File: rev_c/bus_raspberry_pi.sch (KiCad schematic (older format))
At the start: 46 parts, among them J1 TERMINATE_JUMPER, J2 LED_JUMPER, SW1 MJTP1243, U1 MCP7940, U2 74HC08, U3 MCP2562, U4 L78L05AC, U5 ATMEGA324_DIP40, U6 L78L33AC, U7 MCP24XX32A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

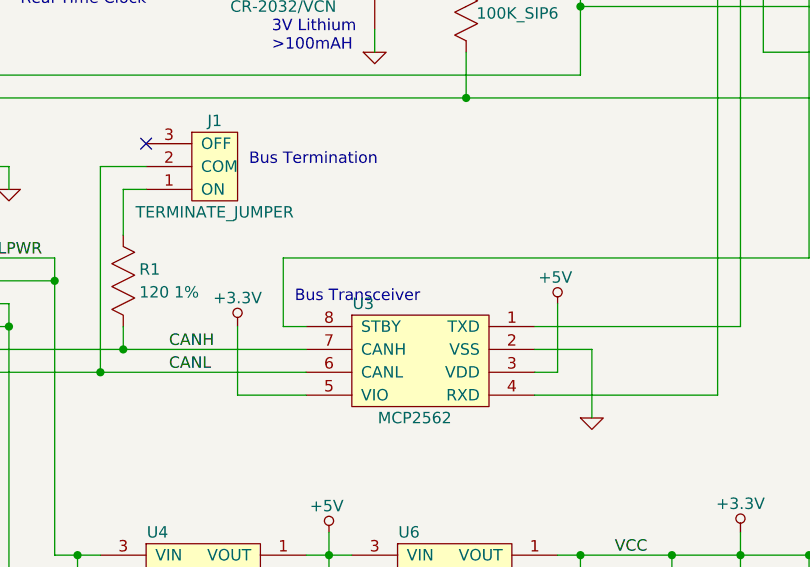
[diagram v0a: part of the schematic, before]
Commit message: Changed from B=>C.  Flipped N1.
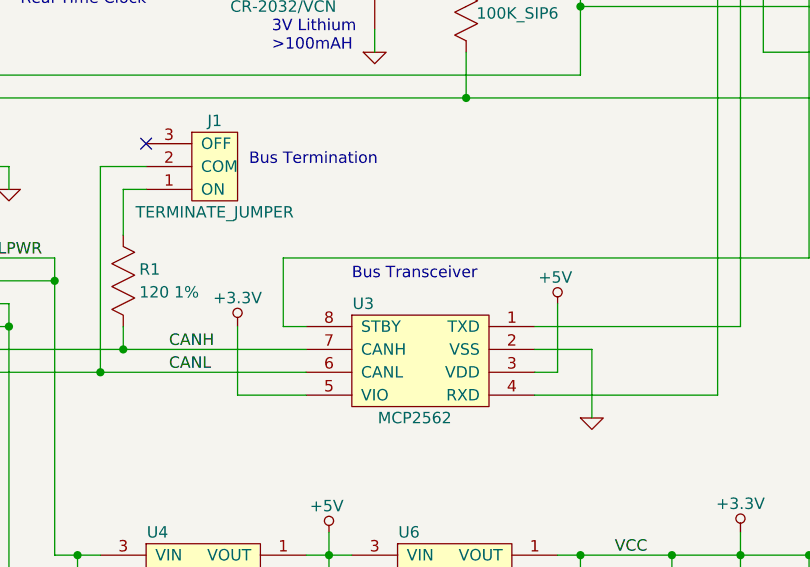
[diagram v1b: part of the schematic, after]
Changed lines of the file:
@@
 Sheet 1 1
 Title "Bus Raspberry Pi"
-Date "Tue 13 Jan 2015"
-Rev "B"
+Date "Sat 31 Jan 2015"
+Rev "C"
 Comp ""
 Comment1 ""
@@
 Text Notes 4500 7800 0    50   ~ 0
 Filter Capacitors
-Text Notes 2650 6000 0    50   ~ 0
+Text Notes 2900 5900 0    50   ~ 0
 Bus Transceiver
 Text Notes 2600 1900 0    50   ~ 0

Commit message: Minor changes to Rev. C.
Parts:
- removed C10: .1uF, bus_raspberry_pi:Capacitor3MMDiscRM2.5, symbol C_HORIZ
- added J3: RESET_SEL, bus_raspberry_pi:Pin_Header_Straight_1x03, symbol RESET_SEL
- added R7: 100K, bus_raspberry_pi:Resistor_Horizontal__400, symbol R_VERT
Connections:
- net +3.3V: now also R7.2; no longer U2.1
- net ~RESET: now also J3.3 (RES); no longer N7.5 (~RESET)
- net at U5.3 (PB2/INT2): now also J3.1 (PGM)
- new net: J3.2 (COM), N7.5 (~RESET)
- new net: R7.1, U2.1
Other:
- moved on the sheet: C6, D1, H5, R2A, R3, U2A
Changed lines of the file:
@@
 Sheet 1 1
 Title "Bus Raspberry Pi"
-Date "Sat 31 Jan 2015"
+Date "Sun 08 Feb 2015"
 Rev "C"
 Comp ""
@@
 L OSHW_LOGO H5
 U 1 1 53E3C102
-P 1000 1100
-F 0 "H5" H 1000 1350 50  0000 C CNN
-F 1 "OSHW_LOGO" H 1000 850 50  0000 C CNN
-F 2 "bus_raspberry_pi:OSHW_LOGO_250mil" H 1000 1100 50  0001 C CNN
-F 3 "" H 1000 1100 50  0000 C CNN
-	1    1000 1100
+P 900 4250
+F 0 "H5" H 900 4500 50  0000 C CNN
+F 1 "OSHW_LOGO" H 900 4000 50  0000 C CNN
+F 2 "bus_raspberry_pi:OSHW_LOGO_250mil" H 900 4250 50  0001 C CNN
+F 3 "" H 900 4250 50  0000 C CNN
+	1    900  4250
 	1    0    0    -1
 $EndComp
@@
 L C_HORIZ C6
 U 1 1 53E3D418
-P 3300 1500
-F 0 "C6" H 3360 1560 50  0000 L CNN
-F 1 ".1uF" H 3360 1430 50  0000 L CNN
-F 2 "bus_raspberry_pi:Capacitor3MMDiscRM2.5" H 3338 1350 30  0001 C CNN
-F 3 "" H 3300 1500 60  0000 C CNN
-	1    3300 1500
+P 3100 1500
+F 0 "C6" H 3160 1560 50  0000 L CNN
+F 1 ".1uF" H 3160 1430 50  0000 L CNN
+F 2 "bus_raspberry_pi:Capacitor3MMDiscRM2.5" H 3138 1350 30  0001 C CNN
+F 3 "" H 3100 1500 60  0000 C CNN
+	1    3100 1500
 	1    0    0    -1
 $EndComp
@@
 L R_VERT R3
 U 1 1 53E3D54A
-P 3600 1200
-F 0 "R3" H 3670 1250 50  0000 L CNN
-F 1 "10K" H 3670 1150 50  0000 L CNN
-F 2 "bus_raspberry_pi:Resistor_Horizontal__400" H 3600 1250 60  0001 C CNN
-F 3 "" H 3600 1250 60  0000 C CNN
-	1    3600 1200
+P 3400 1100
+F 0 "R3" H 3470 1150 50  0000 L CNN
+F 1 "10K" H 3470 1050 50  0000 L CNN
+F 2 "bus_raspberry_pi:Resistor_Horizontal__400" H 3400 1150 60  0001 C CNN
+F 3 "" H 3400 1150 60  0000 C CNN
+	1    3400 1100
 	1    0    0    -1
 $EndComp
@@
 L SCHOTTKY_DIODE_VERT D1
 U 1 1 53E3D5A6
-P 3950 1150
-F 0 "D1" H 3900 1000 50  0000 C CNN
-F 1 "SD101C-TR" H 3700 1250 50  0000 C CNN
-F 2 "bus_raspberry_pi:Diode_DO-41_SOD81_Horizontal_RM10" H 3950 1150 60  0001 C CNN
-F 3 "" H 3950 1150 60  0000 C CNN
-	1    3950 1150
+P 3700 1150
+F 0 "D1" H 3650 1000 50  0000 C CNN
+F 1 "SD101C-TR" H 3450 1250 50  0000 C CNN
+F 2 "bus_raspberry_pi:Diode_DO-41_SOD81_Horizontal_RM10" H 3700 1150 60  0001 C CNN
+F 3 "" H 3700 1150 60  0000 C CNN
+	1    3700 1150
 	-1   0    0    1
 $EndComp
@@
 F 0 "N5" H 850 5950 50  0000 C CNN
 F 1 "FTDI_HEADER" H 950 5125 50  0000 C CNN
-F 2 "bus_raspberry_pi:Pin_Header_Straight_1x06" H 950 5350 60  0001 C CNN
+F 2 "bus_raspberry_pi:Pin_Header_Straight_1x06" H 950 5350 60  0000 C CNN
 F 3 "" H 950 5350 60  0000 C CNN
 	1    950  5350
@@
 NoConn ~ 5600 900
 NoConn ~ 5600 1000
-NoConn ~ 5600 1100
 NoConn ~ 5600 1200
 NoConn ~ 5600 1300
@@
 L 74X08 U2
 U 1 1 53E78B22
-P 2500 1500
-F 0 "U2" H 2500 1750 50  0000 C CNN
-F 1 "74HC08" H 2500 1250 50  0000 C CNN
-F 2 "bus_raspberry_pi:DIP-14__300" H 2500 1500 60  0001 C CNN
-F 3 "" H 2500 1500 60  0000 C CNN
-	1    2500 1500
+P 2300 1500
+F 0 "U2" H 2300 1750 50  0000 C CNN
+F 1 "74HC08" H 2300 1250 50  0000 C CNN
+F 2 "bus_raspberry_pi:DIP-14__300" H 2300 1500 60  0001 C CNN
+F 3 "" H 2300 1500 60  0000 C CNN
+	1    2300 1500
 	1    0    0    -1
 $EndComp
@@
 $EndComp
 $Comp
-L C_HORIZ C10
-U 1 1 53E7ABC3
-P 5700 3300
-F 0 "C10" H 5760 3360 50  0000 L CNN
-F 1 ".1uF" H 5760 3230 50  0000 L CNN
-F 2 "bus_raspberry_pi:Capacitor3MMDiscRM2.5" H 5738 3150 30  0001 C CNN
-F 3 "" H 5700 3300 60  0000 C CNN
-	1    5700 3300
-	1    0    0    -1
-$EndComp
-$Comp
 L C_VERT C5
 U 1 1 53E6ADD9
@@
 L +3.3V #PWR020
 U 1 1 54AE0541
-P 3950 700
-F 0 "#PWR020" H 3950 660 30  0001 C CNN
-F 1 "+3.3V" H 3950 825 50  0000 C CNN
-F 2 "" H 3950 700 60  0000 C CNN
-F 3 "" H 3950 700 60  0000 C CNN
-	1    3950 700
+P 3700 750
+F 0 "#PWR020" H 3700 710 30  0001 C CNN
+F 1 "+3.3V" H 3700 875 50  0000 C CNN
+F 2 "" H 3700 750 60  0000 C CNN
+F 3 "" H 3700 750 60  0000 C CNN
+	1    3700 750
 	1    0    0    -1
 $EndComp
@@
 L +3.3V #PWR021
 U 1 1 54AE0CA5
-P 1400 850
-F 0 "#PWR021" H 1400 810 30  0001 C CNN
-F 1 "+3.3V" H 1400 975 50  0000 C CNN
-F 2 "" H 1400 850 60  0000 C CNN
-F 3 "" H 1400 850 60  0000 C CNN
-	1    1400 850
+P 900 850
+F 0 "#PWR021" H 900 810 30  0001 C CNN
+F 1 "+3.3V" H 900 975 50  0000 C CNN
+F 2 "" H 900 850 60  0000 C CNN
+F 3 "" H 900 850 60  0000 C CNN
+	1    900  850
 	1    0    0    -1
 $EndComp
@@
 L R_VERT_SIP6 R2
 U 1 1 54B3786F
-P 1400 1150
-F 0 "R2" H 1445 1220 50  0000 L CNN
-F 1 "100K_SIP6" H 1445 1120 50  0000 L CNN
-F 2 "bus_raspberry_pi:Pin_Header_Straight_1x06" H 1400 1150 50  0001 C CNN
-F 3 "" H 1400 1150 50  0000 C CNN
-	1    1400 1150
+P 900 1150
+F 0 "R2" H 945 1220 50  0000 L CNN
+F 1 "100K_SIP6" H 945 1120 50  0000 L CNN
+F 2 "bus_raspberry_pi:Pin_Header_Straight_1x06" H 900 1150 50  0001 C CNN
+F 3 "" H 900 1150 50  0000 C CNN
+	1    900  1150
 	1    0    0    -1
 $EndComp
@@
 Connection ~ 1400 2100
 Wire Wire Line
-	3950 700  3950 900
-Wire Wire Line
-	3600 1000 3600 800
-Wire Wire Line
-	3950 1500 3950 1400
-Wire Wire Line
-	3600 1400 3600 1500
-Connection ~ 3600 1500
-Connection ~ 3950 1500
+	3700 750  3700 900
+Wire Wire Line
+	3400 900  3400 800
+Wire Wire Line
+	3700 1500 3700 1400
+Wire Wire Line
+	3400 1300 3400 1500
+Connection ~ 3400 1500
+Connection ~ 3700 1500
 Wire Wire Line
 	1300 6100 1400 6100
@@
 	9100 3300 9400 3300
 Wire Wire Line
-	3500 1500 4300 1500
+	3300 1500 4300 1500
 Wire Wire Line
 	9200 3500 9200 6200
@@
 Wire Wire Line
 	4300 1700 5600 1700
-Connection ~ 3950 800
+Connection ~ 3700 800
 Wire Wire Line
 	5600 1800 5500 1800
@@
 	5000 1400 5600 1400
 Wire Wire Line
-	4800 1700 4800 4100
-Connection ~ 4800 1700
-Wire Wire Line
 	5200 1600 5600 1600
 Wire Wire Line
@@
 	8000 1400 8200 1400
 Wire Wire Line
-	3000 1500 3100 1500
+	2800 1500 2900 1500
 Wire Wire Line
 	5200 3000 8000 3000
@@
 Wire Wire Line
 	5400 4200 5400 4300
-Wire Wire Line
-	5900 3300 6300 3300
 Wire Wire Line
 	5500 3900 5200 3900
@@
 	4400 2500 4300 2500
 Wire Wire Line
-	1400 950  1400 850
+	900  950  900  850
 Wire Wire Line
 	6100 5900 5800 5900
@@
 Wire Wire Line
 	4800 4100 5500 4100
-Connection ~ 4800 3300
 Wire Wire Line
 	4900 7100 4900 7200
@@
 	5500 1800 5500 800
 Wire Wire Line
-	5500 800  1900 800
-Wire Wire Line
-	1400 1600 2000 1600
-Wire Wire Line
-	2000 1400 1900 1400
-Wire Wire Line
-	1900 1400 1900 800
-Connection ~ 3600 800
+	5500 800  1700 800
+Wire Wire Line
+	900  1600 1800 1600
+Wire Wire Line
+	1800 1400 1700 1400
+Connection ~ 3400 800
 Wire Wire Line
 	7300 3200 8700 3200
-Wire Wire Line
-	5500 3300 4800 3300
 Wire Wire Line
 	9000 6100 8300 6100
@@
 	2000 3300 2000 2800
 Wire Wire Line
-	1400 1600 1400 1350
+	900  1600 900  1350
 Wire Wire Line
 	5600 2800 4900 2800
@@
 NoConn ~ 9200 1500
 NoConn ~ 9200 1900
+NoConn ~ 6300 3300
+$Comp
+L RESET_SEL J3
+U 1 1 54D83853
+P 4300 1200
+F 0 "J3" H 4250 1400 50  0000 C CNN
+F 1 "RESET_SEL" H 4300 1000 50  0000 C CNN
+F 2 "bus_raspberry_pi:Pin_Header_Straight_1x03" H 4300 1200 60  0001 C CNN
+F 3 "" H 4300 1200 60  0000 C CNN
+	1    4300 1200
+	1    0    0    -1
+$EndComp
+Wire Wire Line
+	4800 4100 4800 1200
+Wire Wire Line
+	4800 1200 4600 1200
+Wire Wire Line
+	4600 1300 4700 1300
+Wire Wire Line
+	4700 1300 4700 1700
+Connection ~ 4700 1700
+Wire Wire Line
+	4600 1100 5600 1100
+$Comp
+L R_VERT R7
+U 1 1 54D84A4A
+P 1700 1100
+F 0 "R7" H 1770 1150 50  0000 L CNN
+F 1 "100K" H 1770 1050 50  0000 L CNN
+F 2 "bus_raspberry_pi:Resistor_Horizontal__400" H 1700 1150 60  0001 C CNN
+F 3 "" H 1700 1150 60  0000 C CNN
+	1    1700 1100
+	1    0    0    -1
+$EndComp
+Wire Wire Line
+	1700 800  1700 900
+Wire Wire Line
+	1700 1400 1700 1300
 $EndSCHEMATC
